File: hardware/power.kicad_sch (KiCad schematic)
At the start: 38 parts, among them U1 INA186A3, U2 TPS61022, U24 SGM40661, U3 TPS2116, U4 LP5912-3.3, U5 TPS22810

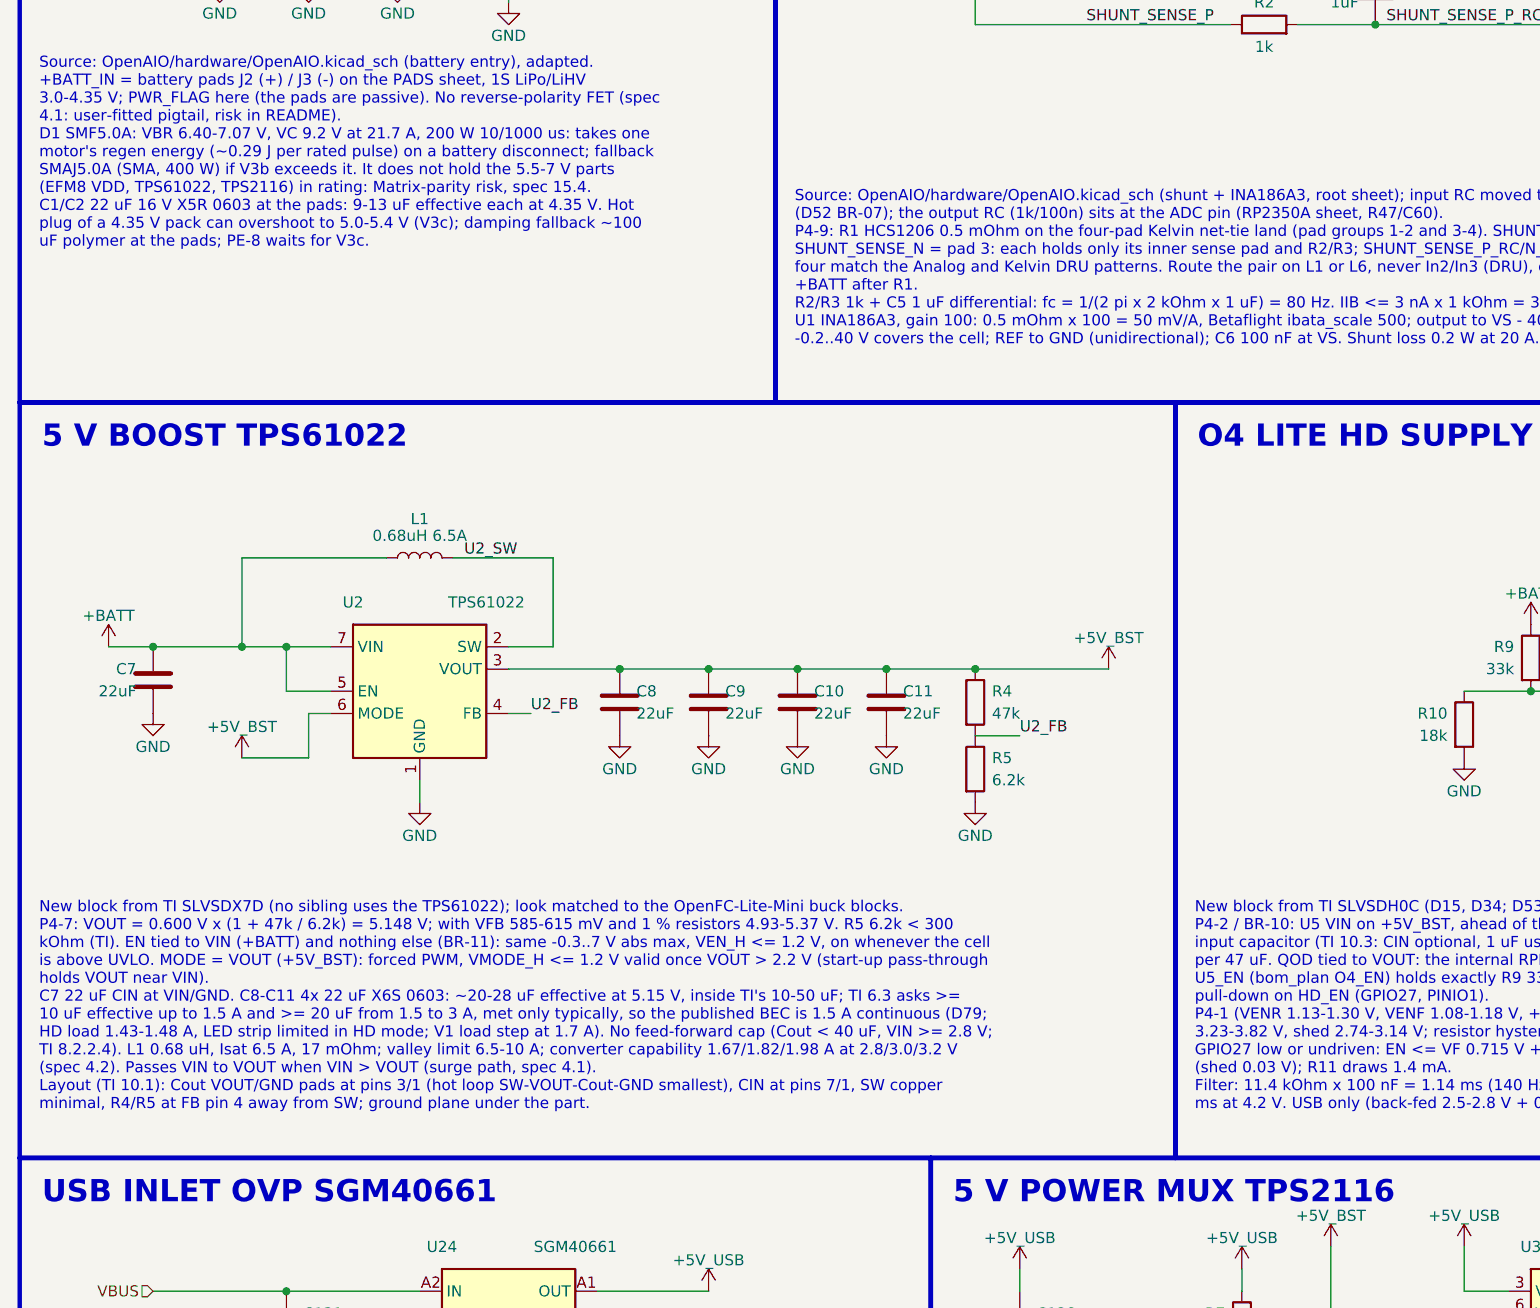
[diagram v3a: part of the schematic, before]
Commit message: hardware: floorplan v3 review pass (RX RF corner blocker fixed; majors listed in FLOORPLAN.md Open)
Co-Authored-By: Claude Opus 5.5 <noreply@anthropic.com>
Claude-Session: https://claude.ai/code/session_01RFaS5jnC9tnPam9GBgmGnG
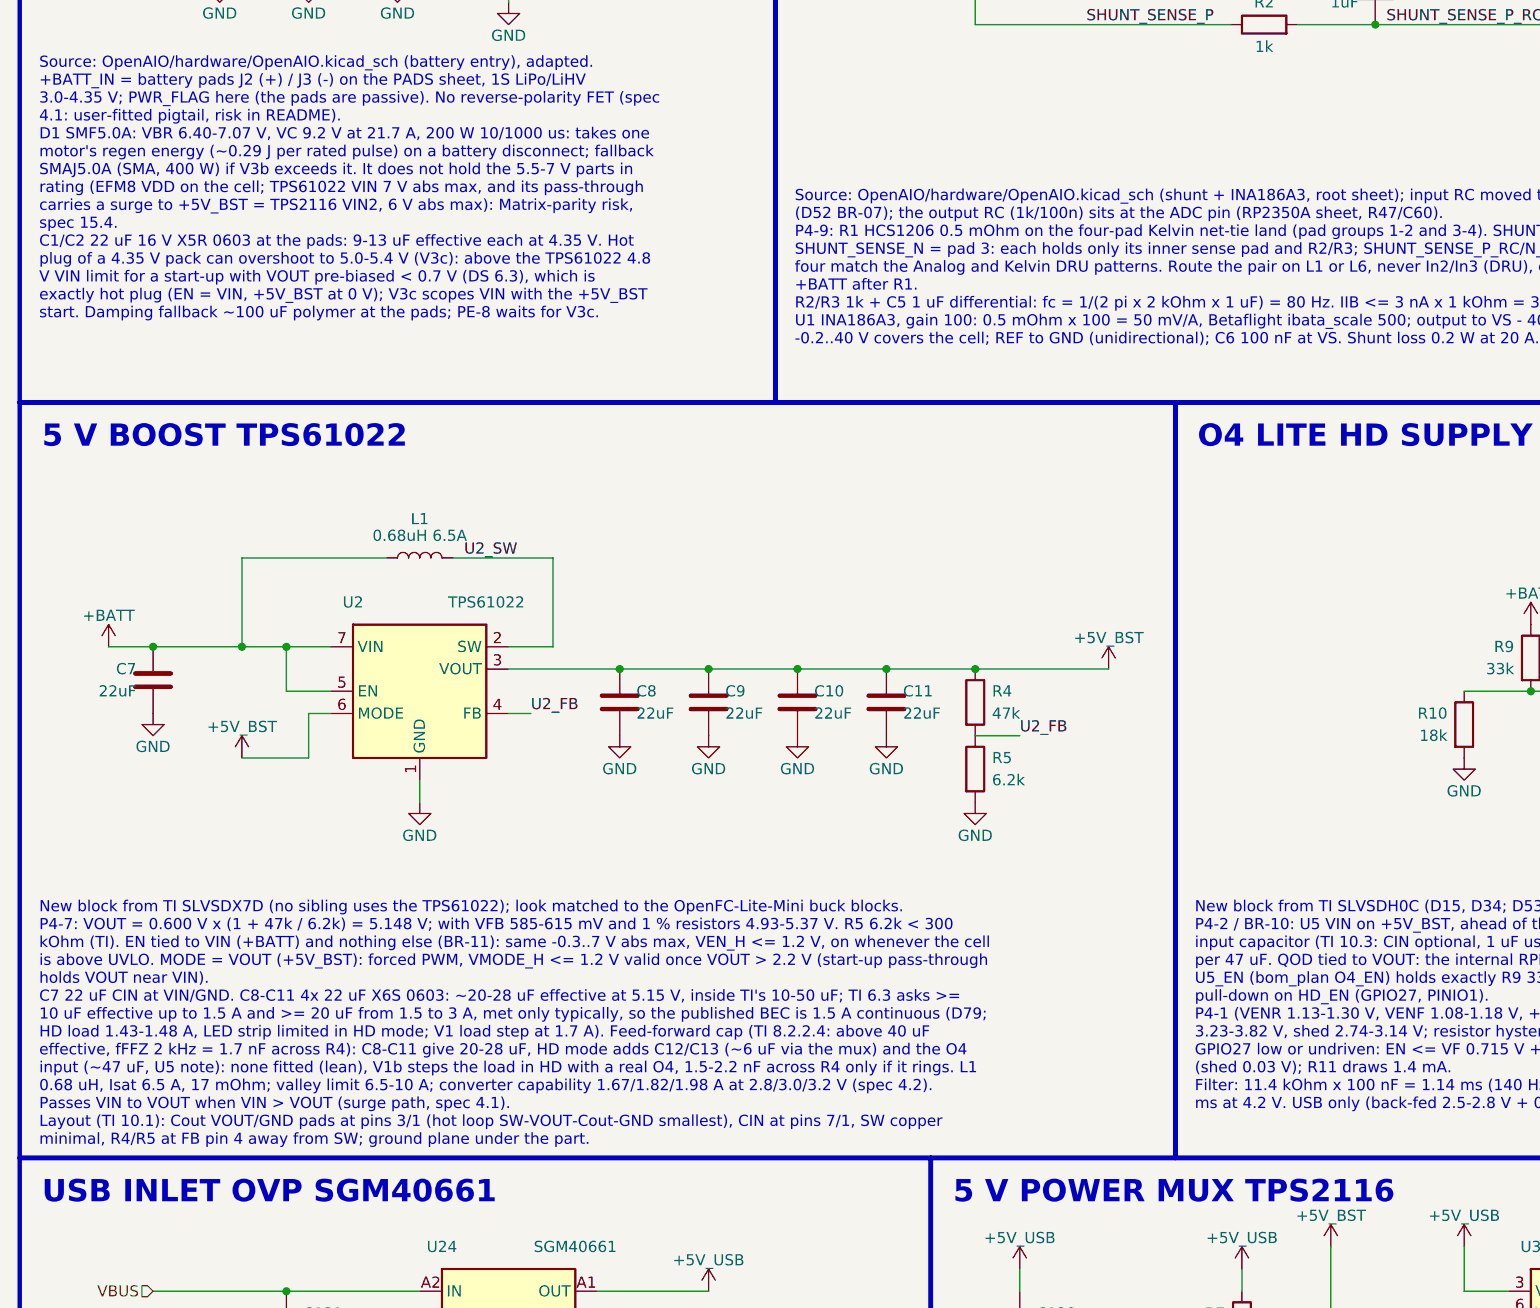
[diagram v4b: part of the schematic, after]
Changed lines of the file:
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@@
 		)
 	)
-	(text_box "Source: OpenAIO/hardware/OpenAIO.kicad_sch (battery entry), adapted.\n+BATT_IN = battery pads J2 (+) / J3 (-) on the PADS sheet, 1S LiPo/LiHV 3.0-4.35 V; PWR_FLAG here (the pads are passive). No reverse-polarity FET (spec 4.1: user-fitted pigtail, risk in README).\nD1 SMF5.0A: VBR 6.40-7.07 V, VC 9.2 V at 21.7 A, 200 W 10/1000 us: takes one motor's regen energy (~0.29 J per rated pulse) on a battery disconnect; fallback SMAJ5.0A (SMA, 400 W) if V3b exceeds it. It does not hold the 5.5-7 V parts (EFM8 VDD, TPS61022, TPS2116) in rating: Matrix-parity risk, spec 15.4.\nC1/C2 22 uF 16 V X5R 0603 at the pads: 9-13 uF effective each at 4.35 V. Hot plug of a 4.35 V pack can overshoot to 5.0-5.4 V (V3c); damping fallback ~100 uF polymer at the pads; PE-8 waits for V3c."
+	(text_box "Source: OpenAIO/hardware/OpenAIO.kicad_sch (battery entry), adapted.\n+BATT_IN = battery pads J2 (+) / J3 (-) on the PADS sheet, 1S LiPo/LiHV 3.0-4.35 V; PWR_FLAG here (the pads are passive). No reverse-polarity FET (spec 4.1: user-fitted pigtail, risk in README).\nD1 SMF5.0A: VBR 6.40-7.07 V, VC 9.2 V at 21.7 A, 200 W 10/1000 us: takes one motor's regen energy (~0.29 J per rated pulse) on a battery disconnect; fallback SMAJ5.0A (SMA, 400 W) if V3b exceeds it. It does not hold the 5.5-7 V parts in rating (EFM8 VDD on the cell; TPS61022 VIN 7 V abs max, and its pass-through carries a surge to +5V_BST = TPS2116 VIN2, 6 V abs max): Matrix-parity risk, spec 15.4.\nC1/C2 22 uF 16 V X5R 0603 at the pads: 9-13 uF effective each at 4.35 V. Hot plug of a 4.35 V pack can overshoot to 5.0-5.4 V (V3c): above the TPS61022 4.8 V VIN limit for a start-up with VOUT pre-biased < 0.7 V (DS 6.3), which is exactly hot plug (EN = VIN, +5V_BST at 0 V); V3c scopes VIN with the +5V_BST start. Damping fallback ~100 uF polymer at the pads; PE-8 waits for V3c."
 		(exclude_from_sim no)
 		(at 16.51 55.88 0)
@@
 		)
 	)
-	(text_box "New block from TI SLVSDX7D (no sibling uses the TPS61022); look matched to the OpenFC-Lite-Mini buck blocks.\nP4-7: VOUT = 0.600 V x (1 + 47k / 6.2k) = 5.148 V; with VFB 585-615 mV and 1 % resistors 4.93-5.37 V. R5 6.2k < 300 kOhm (TI). EN tied to VIN (+BATT) and nothing else (BR-11): same -0.3..7 V abs max, VEN_H <= 1.2 V, on whenever the cell is above UVLO. MODE = VOUT (+5V_BST): forced PWM, VMODE_H <= 1.2 V valid once VOUT > 2.2 V (start-up pass-through holds VOUT near VIN).\nC7 22 uF CIN at VIN/GND. C8-C11 4x 22 uF X6S 0603: ~20-28 uF effective at 5.15 V, inside TI's 10-50 uF; TI 6.3 asks >= 10 uF effective up to 1.5 A and >= 20 uF from 1.5 to 3 A, met only typically, so the published BEC is 1.5 A continuous (D79; HD load 1.43-1.48 A, LED strip limited in HD mode; V1 load step at 1.7 A). No feed-forward cap (Cout < 40 uF, VIN >= 2.8 V; TI 8.2.2.4). L1 0.68 uH, Isat 6.5 A, 17 mOhm; valley limit 6.5-10 A; converter capability 1.67/1.82/1.98 A at 2.8/3.0/3.2 V (spec 4.2). Passes VIN to VOUT when VIN > VOUT (surge path, spec 4.1).\nLayout (TI 10.1): Cout VOUT/GND pads at pins 3/1 (hot loop SW-VOUT-Cout-GND smallest), CIN at pins 7/1, SW copper minimal, R4/R5 at FB pin 4 away from SW; ground plane under the part."
+	(text_box "New block from TI SLVSDX7D (no sibling uses the TPS61022); look matched to the OpenFC-Lite-Mini buck blocks.\nP4-7: VOUT = 0.600 V x (1 + 47k / 6.2k) = 5.148 V; with VFB 585-615 mV and 1 % resistors 4.93-5.37 V. R5 6.2k < 300 kOhm (TI). EN tied to VIN (+BATT) and nothing else (BR-11): same -0.3..7 V abs max, VEN_H <= 1.2 V, on whenever the cell is above UVLO. MODE = VOUT (+5V_BST): forced PWM, VMODE_H <= 1.2 V valid once VOUT > 2.2 V (start-up pass-through holds VOUT near VIN).\nC7 22 uF CIN at VIN/GND. C8-C11 4x 22 uF X6S 0603: ~20-28 uF effective at 5.15 V, inside TI's 10-50 uF; TI 6.3 asks >= 10 uF effective up to 1.5 A and >= 20 uF from 1.5 to 3 A, met only typically, so the published BEC is 1.5 A continuous (D79; HD load 1.43-1.48 A, LED strip limited in HD mode; V1 load step at 1.7 A). Feed-forward cap (TI 8.2.2.4: above 40 uF effective, fFFZ 2 kHz = 1.7 nF across R4): C8-C11 give 20-28 uF, HD mode adds C12/C13 (~6 uF via the mux) and the O4 input (~47 uF, U5 note): none fitted (lean), V1b steps the load in HD with a real O4, 1.5-2.2 nF across R4 only if it rings. L1 0.68 uH, Isat 6.5 A, 17 mOhm; valley limit 6.5-10 A; converter capability 1.67/1.82/1.98 A at 2.8/3.0/3.2 V (spec 4.2). Passes VIN to VOUT when VIN > VOUT (surge path, spec 4.1).\nLayout (TI 10.1): Cout VOUT/GND pads at pins 3/1 (hot loop SW-VOUT-Cout-GND smallest), CIN at pins 7/1, SW copper minimal, R4/R5 at FB pin 4 away from SW; ground plane under the part."
 		(exclude_from_sim no)
 		(at 16.51 152.4 0)
@@
 		(length 2.54)
 		(shape round)
+		(at 76.2 114.3 0)
+		(fields_autoplaced yes)
+		(effects
+			(font
+				(size 1.27 1.27)
+			)
+			(justify left bottom)
+		)
+		(property "Netclass" "Phase"
+			(at 77.47 110.49 0)
+			(show_name no)
+			(do_not_autoplace no)
+			(effects
+				(font
+					(size 1.27 1.27)
+					(italic yes)
+				)
+				(justify left)
+			)
+		)
+	)
+	(netclass_flag ""
+		(length 2.54)
+		(shape round)
 		(at 127 127 0)
 		(fields_autoplaced yes)
@@
 			)
 		)
-		(property "Description" "SG Micro SGM40661 OVP load switch, WLCSP-6: IN 28 V abs max, 2.7-20 V recommended (feature list: 40 V surge immunity), OVLO tied to GND = internal 5.75-6.12 V trip, 4 A, 27/45 mOhm (SGM40659/60/61 DS REV.A, absolute maximum ratings and recommended operating conditions)"
+		(property "Description" "SG Micro SGM40661 OVP load switch, WLCSP-6: IN 28 V abs max, 2.7-20 V recommended (feature list: 40 V surge immunity), OVLO tied to GND = internal 5.75-6.12 V trip, 3 A continuous (recommended operating), 4 A abs max, 27/45 mOhm (SGM40659/60/61 DS REV.A, absolute maximum ratings and recommended operating conditions)"
 			(at 71.12 200.66 0)
 			(hide yes)

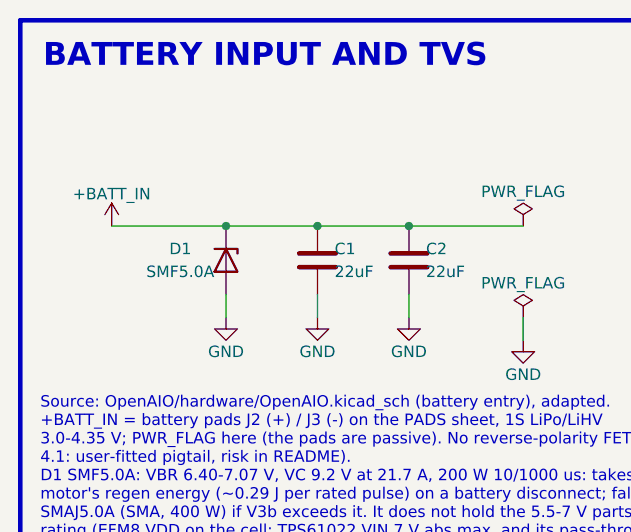
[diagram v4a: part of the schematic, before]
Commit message: wip: routing prep (zones and via fields) and schematic review round 4
Co-Authored-By: Claude Opus 5.5 <noreply@anthropic.com>
Claude-Session: https://claude.ai/code/session_01RFaS5jnC9tnPam9GBgmGnG
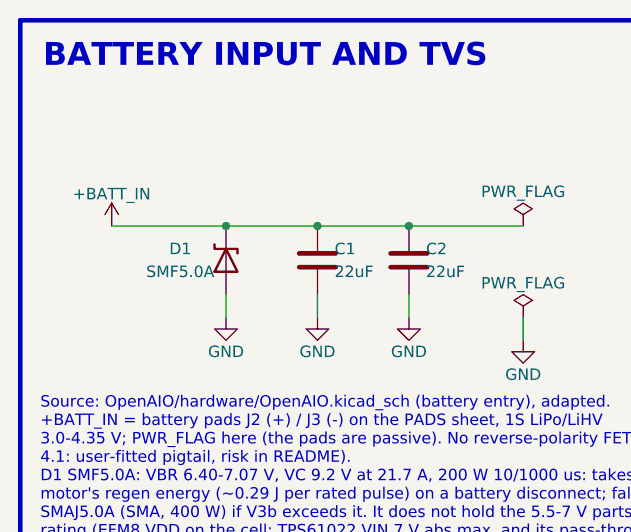
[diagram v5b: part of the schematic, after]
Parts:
- D1: symbol Device:D_Zener -> lib:SMF5.0A
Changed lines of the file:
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@@
 	)
 	(symbol
-		(lib_id "Device:D_Zener")
+		(lib_id "lib:SMF5.0A")
 		(at 38.1 41.91 270)
 		(unit 1)
@@
 			)
 		)
-		(property "Description" "Zener diode"
+		(property "Description" "Unidirectional TVS diode, VRWM 5.0 V, VBR 6.40-7.07 V, 200 W (10/1000 us), SOD-123FL; Littelfuse SMF series. Pin 1 K, pin 2 A"
 			(at 38.1 41.91 0)
 			(hide yes)
